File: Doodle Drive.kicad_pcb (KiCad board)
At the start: 2 copper layers, 69.1 x 82.1 mm, 99 parts, among them J1 USB_B, J12 PINHD_1x4_Male, J15 PINHD_1x4_Male, J2 USB_B, J3 Screw_Terminal_01x02, J4 PINHD_1x4_Male, J5 USB_A, J6 PINHD_1x2_Male, J8 PINHD_1x4_Male, J9 PINHD_1x4_Male, U1 STM32F411RETx, U2 DRV8825PWP, U3 DRV8825PWP, U4 DRV8825PWP, U5 DRV8825PWP, U6 AP7343-33W5-7, U7 CP2102-GMR, Y1 32.768KHz ±20ppm 12.5pF, Y2 25MHZ 12PF

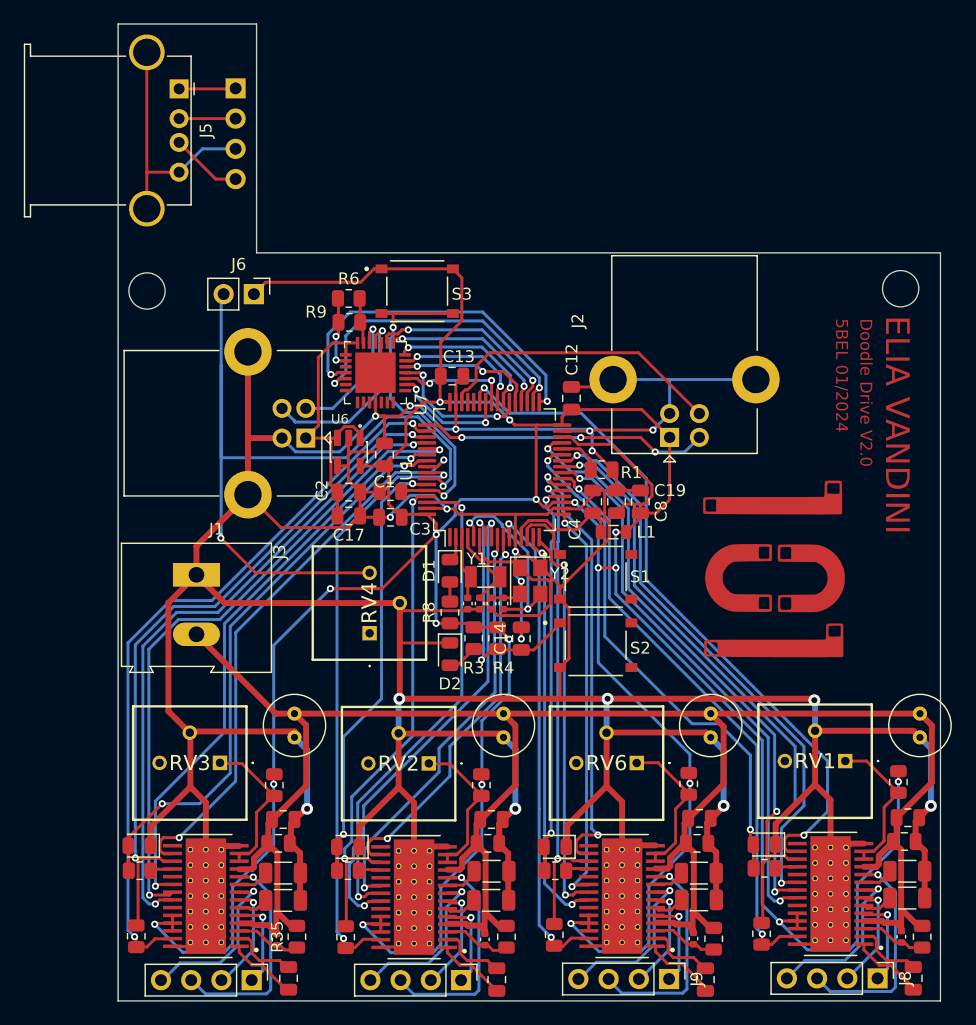
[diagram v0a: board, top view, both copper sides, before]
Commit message: added pins for motor edge sensors, reroutet driver modules, removed module potentiometer, made everything more compact, fixed labels
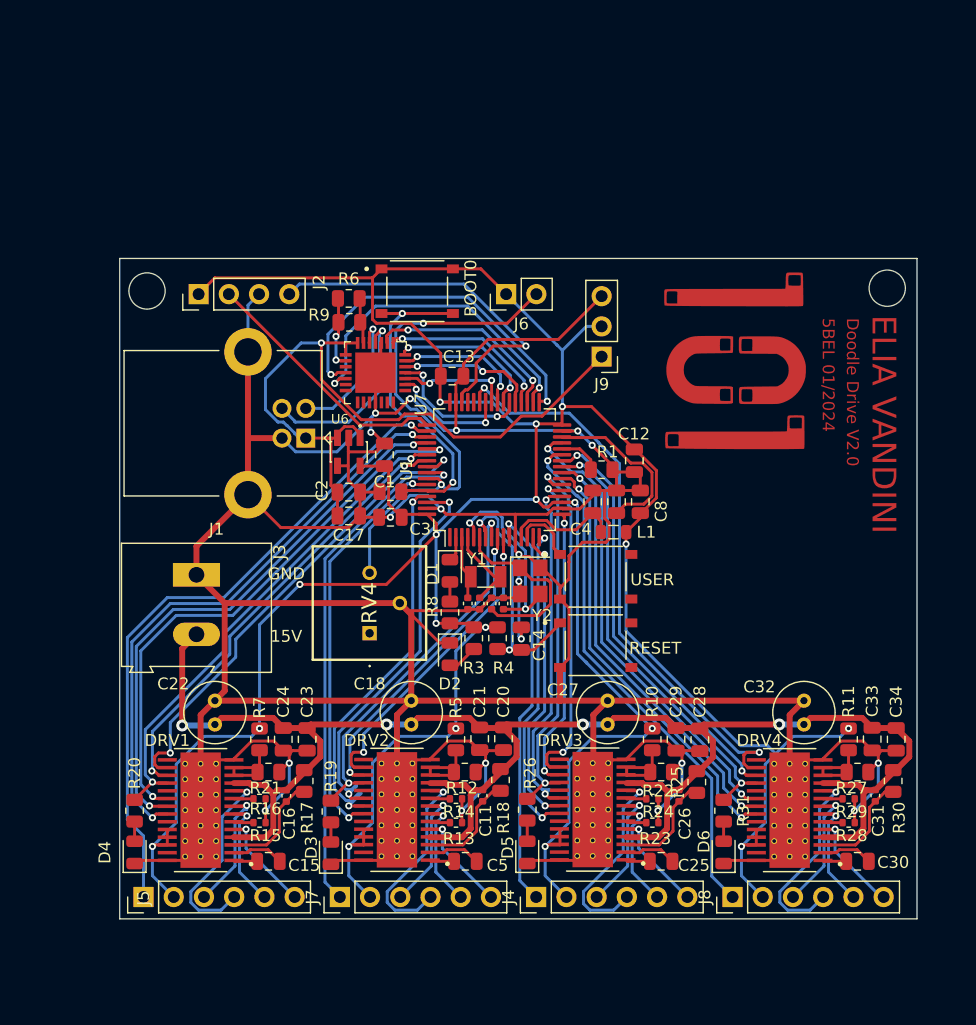
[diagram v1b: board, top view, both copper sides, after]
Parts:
- removed J12, J15: PINHD_1x4_Male, Connector_PinHeader_2.54mm:PinHeader_1x04_P2.54mm_Vertical
- removed R33, R34: 0.1, Resistor_SMD:R_1206_3216Metric
- removed R35: 1M, Resistor_SMD:R_0805_2012Metric
- removed R39: 10k, Resistor_SMD:R_0805_2012Metric
- removed R40: 5.1k, Resistor_SMD:R_0805_2012Metric
- removed RV1, RV2, RV3, RV6: R_Potentiometer, poti:3386P1473LF
- removed U2, U3, U4, U5: DRV8825PWP, DRV8825PWP:IC_TPS61196PWPRQ1
- added DRV1: DRV8825PWP, DRV8825PWP:IC_TPS61196PWPRQ1, F.Cu at (68.0, 98.1)
- added DRV2: DRV8825PWP, DRV8825PWP:IC_TPS61196PWPRQ1, F.Cu at (84.5, 98.1)
- added DRV3: DRV8825PWP, DRV8825PWP:IC_TPS61196PWPRQ1, F.Cu at (101.0, 98.1)
- added DRV4: DRV8825PWP, DRV8825PWP:IC_TPS61196PWPRQ1, F.Cu at (117.5, 98.1)
- added J7: PINHD_1x6_Male, Connector_PinHeader_2.54mm:PinHeader_1x06_P2.54mm_Vertical, F.Cu at (79.8, 105.4)
- added R20: 5.1k, Resistor_SMD:R_0805_2012Metric, F.Cu at (62.5, 98.2)
- added R23: 200m, Resistor_SMD:R_0402_1005Metric, F.Cu at (106.0, 99.2)
- added R27: 10k, Resistor_SMD:R_0805_2012Metric, F.Cu at (123.2, 94.9)
- added R28: 200m, Resistor_SMD:R_0402_1005Metric, F.Cu at (122.5, 99.2)
- added R29: 200m, Resistor_SMD:R_0402_1005Metric, F.Cu at (122.5, 97.2)
- J2: value USB_B -> PINHD_1x4_Male; footprint Connector_USB:USB_B_Lumberg_2411_02_Horizontal -> Connector_PinHeader_2.54mm:PinHeader_1x04_P2.54mm_Vertical
- J4: value PINHD_1x4_Male -> PINHD_1x6_Male; footprint Connector_PinHeader_2.54mm:PinHeader_1x04_P2.54mm_Vertical -> Connector_PinHeader_2.54mm:PinHeader_1x06_P2.54mm_Vertical; moved to F.Cu
- J5: value USB_A -> PINHD_1x6_Male; footprint Connector_USB:USB_A_Stewart_SS-52100-001_Horizontal -> Connector_PinHeader_2.54mm:PinHeader_1x06_P2.54mm_Vertical
- J8: value PINHD_1x4_Male -> PINHD_1x6_Male; footprint Connector_PinHeader_2.54mm:PinHeader_1x04_P2.54mm_Vertical -> Connector_PinHeader_2.54mm:PinHeader_1x06_P2.54mm_Vertical
- J9: value PINHD_1x4_Male -> PINHD_1x3_Male; footprint Connector_PinHeader_2.54mm:PinHeader_1x04_P2.54mm_Vertical -> Connector_PinHeader_2.54mm:PinHeader_1x03_P2.54mm_Vertical
- R10, R11, R5, R7: value 1k -> 3.6k
- R12: value 0.1 -> 10k; footprint Resistor_SMD:R_1206_3216Metric -> Resistor_SMD:R_0805_2012Metric
- R13, R15, R16, R24: value 0.1 -> 200m; footprint Resistor_SMD:R_1206_3216Metric -> Resistor_SMD:R_0402_1005Metric
- R14: value 1M -> 200m; footprint Resistor_SMD:R_0805_2012Metric -> Resistor_SMD:R_0402_1005Metric
- R18, R30: value 10k -> 1M
- R22: value 5.1k -> 10k
- R25: value 0.1 -> 1M; footprint Resistor_SMD:R_1206_3216Metric -> Resistor_SMD:R_0805_2012Metric
- R26: value 1M -> 5.1k
- R8: value 1k -> 5.1k
- moved J4 72.5 mm to (96.2, 105.4), turned to 90 degrees
- moved J5 68.0 mm to (63.2, 105.4), turned to 90 degrees
- moved C34 52.6 mm to (126.5, 92.2), turned to -90 degrees
- moved J9 52.6 mm to (101.8, 60.0), turned to 180 degrees
- moved C31 51.7 mm to (124.8, 96.9)
- moved C33 50.0 mm to (124.5, 92.1), turned to -90 degrees
- moved D6 49.1 mm to (112.0, 101.7), turned to 90 degrees
- moved C30 48.8 mm to (123.2, 102.4), turned to 180 degrees
- moved R11 48.4 mm to (122.5, 92.2)
- moved R30 47.8 mm to (126.2, 95.7), turned to 90 degrees
- moved C32 42.9 mm to (118.8, 88.9), turned to -90 degrees
- moved C18 42.9 mm to (85.8, 88.9), turned to -90 degrees
- moved C22 41.8 mm to (69.2, 88.9), turned to -90 degrees
- moved J2 41.4 mm to (67.9, 54.8)
- moved R14 40.9 mm to (89.5, 97.2), turned to 0 degrees
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- renumbered S3 to BOOT0, S2 to RESET, S1 to USER
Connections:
- C11 pad 2: Net-(U2-VCP) -> Net-(DRV2-VCP)
- C26 pad 2: Net-(U4-VCP) -> Net-(DRV3-VCP)
- C31 pad 2: Net-(U5-VCP) -> Net-(DRV4-VCP)
- C6 pad 2: PH1 -> PH0
- C9 pad 2: PH0 -> PH1
- D3 pad 2: PB1 -> Net-(D3-A)
- D4 pad 2: PA4 -> Net-(D4-A)
- D5 pad 2: PB7 -> Net-(D5-A)
- D6 pad 2: PB3 -> Net-(D6-A)
- J2 pad 3: PA13 -> GND
- J2 pad 4: GND -> PA13
- J4 pad 1: Net-(J5-VBUS) -> PC3
- J4 pad 2: Net-(J5-D-) -> +3V3
- J4 pad 3: Net-(J5-GND) -> Net-(DRV3-BOUT2)
- J4 pad 4: Net-(J5-D+) -> Net-(DRV3-BOUT1)
- J5 pad 1: Net-(J5-VBUS) -> PA15
- J5 pad 2: Net-(J5-D-) -> +3V3
- J5 pad 3: Net-(J5-D+) -> Net-(DRV1-BOUT2)
- J5 pad 4: Net-(J5-GND) -> Net-(DRV1-BOUT1)
- J5 pad 5: Net-(J5-GND) -> Net-(DRV1-AOUT2)
- J8 pad 1: Net-(U2-AOUT1) -> PB1
- J8 pad 2: Net-(U2-AOUT2) -> +3V3
- J9 pad 1: Net-(U3-AOUT1) -> +5V
- J9 pad 2: Net-(U3-AOUT2) -> +3V3
- J9 pad 3: Net-(U3-BOUT1) -> GND
- R10 pad 1: Net-(U4-AVREF) -> Net-(DRV3-AVREF)
- R12 pad 1: Net-(U2-ISENA) -> GND
- R12 pad 2: GND -> Net-(DRV2-AVREF)
- R13 pad 1: GND -> Net-(DRV2-ISENA)
- R13 pad 2: Net-(U2-ISENB) -> GND
- R14 pad 1: Net-(U2-VCP) -> Net-(DRV2-ISENB)
- R14 pad 2: +15V -> GND
- R16 pad 1: GND -> Net-(DRV1-ISENB)
- R16 pad 2: Net-(U3-ISENB) -> GND
- R18 pad 1: PB10 -> Net-(DRV2-VCP)
- R18 pad 2: PA7 -> +15V
- R19 pad 1: PB1 -> PC0
- R19 pad 2: Net-(U2-NFAULT) -> Net-(D3-A)
- R21 pad 1: PA5 -> GND
- R21 pad 2: PC3 -> Net-(DRV1-AVREF)
- R22 pad 1: PA4 -> GND
- R22 pad 2: Net-(U3-NFAULT) -> Net-(DRV3-AVREF)
- R25 pad 1: GND -> Net-(DRV3-VCP)
- R25 pad 2: Net-(U4-ISENB) -> +15V
- R26 pad 1: Net-(U4-VCP) -> PA5
- R26 pad 2: +15V -> Net-(D5-A)
- R30 pad 1: PB8 -> Net-(DRV4-VCP)
- R30 pad 2: PB5 -> +15V
- R31 pad 1: PB7 -> PC5
- R31 pad 2: Net-(U4-NFAULT) -> Net-(D6-A)
- R5 pad 1: Net-(U2-AVREF) -> Net-(DRV2-AVREF)
- R7 pad 1: Net-(U3-AVREF) -> Net-(DRV1-AVREF)
- U1 pad 17: DIR1 -> PA3
- U1 pad 20: PA4 -> DIR3
- U1 pad 26: DIR2 -> PB0
- U1 pad 29: PB10 -> DIR4
- U1 pad 53: PC12 -> DIR1
- U1 pad 54: DIR4 -> PD2
- U1 pad 62: PB9 -> DIR2
- U1 pad 9: DIR3 -> PC1
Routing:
- net PC12: track 55.2 -> 0.00 mm, vias 2 -> 0
- net PB10: track 53.5 -> 0.00 mm, vias 2 -> 0
- net GND: track 505.2 -> 454.0 mm, vias 18 -> 19
- net PB9: track 42.9 -> 0.00 mm, vias 2 -> 0
- net PD2: track 0.00 -> 42.1 mm, vias 0 -> 2
- net +15V: track 184.5 -> 145.5 mm, vias 0 -> 4
- net +5V: track 25.2 -> 62.0 mm, vias 0 -> 1
- net PB0: track 0.00 -> 35.3 mm, vias 0 -> 2
- net PA4: track 35.2 -> 0.00 mm, vias 2 -> 0
- net PC1: track 0.00 -> 26.1 mm, vias 0 -> 2
- net PB6: track 69.0 -> 43.0 mm
- net PA3: track 0.00 -> 23.7 mm, vias 0 -> 2
- net +3V3: track 334.0 -> 310.8 mm, vias 19 -> 18
- net Net-(J5-GND): track 21.4 -> 0.00 mm
- net Net-(U3-BOUT1): track 18.4 -> 0.00 mm, vias 1 -> 0
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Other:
- board size 69.1 x 82.1 mm -> 67 x 55.5 mm
- board text added: "15V"
- board text added: "5V"
- board text added: "AOUT1"
- board text added: "AOUT2"
- board text added: "BOUT1"
- board text added: "BOUT2"
- board text added: "SENSOR"
- board text removed: "CKL"
- board text removed: "IO"
- board text removed: "SWIO"
- board text removed: "TOP"

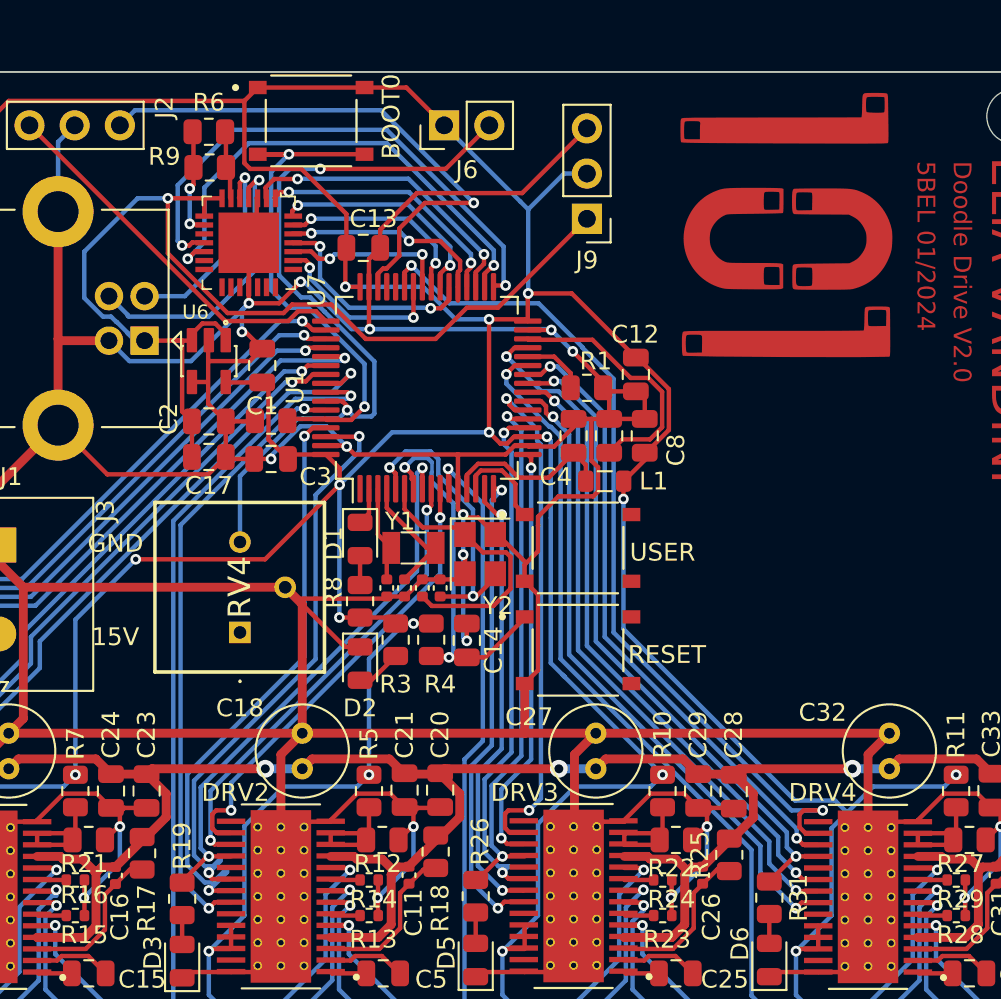
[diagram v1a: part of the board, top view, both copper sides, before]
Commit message: fixed Serial connection, and various improvments
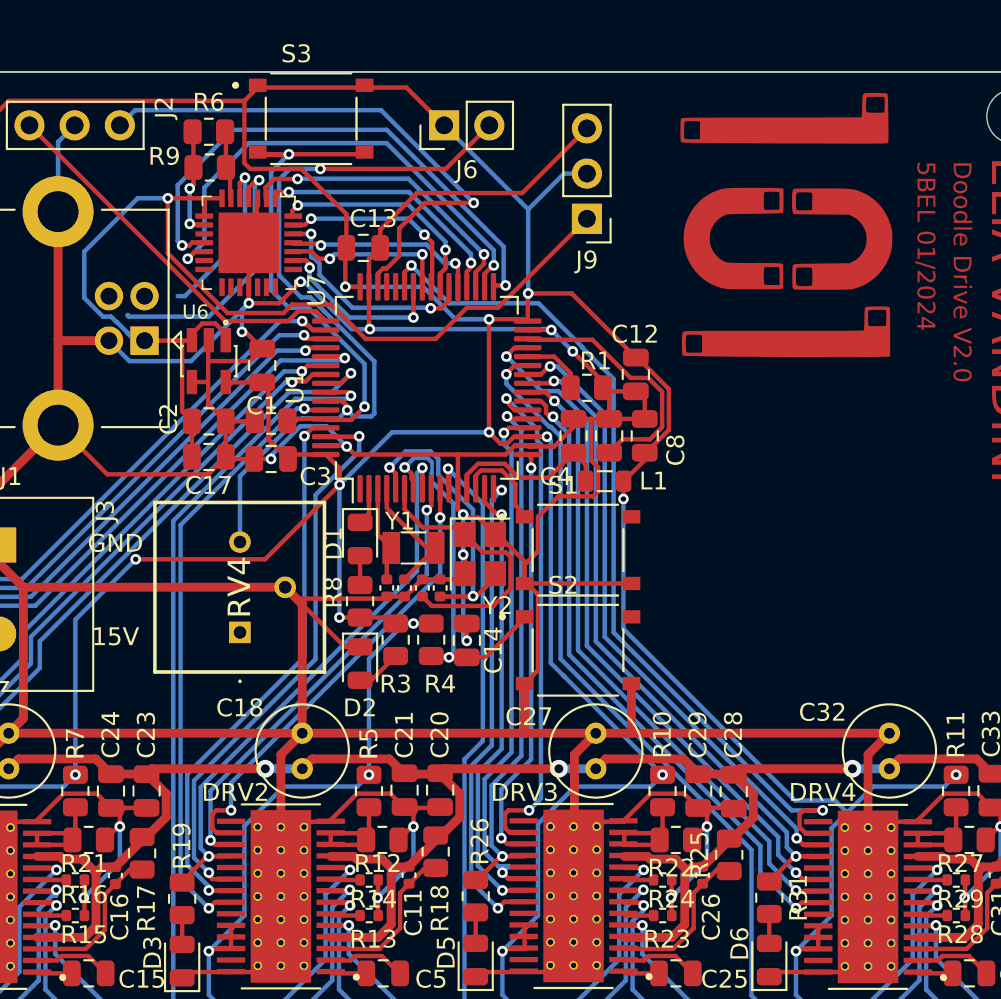
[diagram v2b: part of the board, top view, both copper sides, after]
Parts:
- removed BOOT0, RESET, USER: TS-1187A-B-A-B, TS-1187A-B-A-B:SW_TS-1187A-B-A-B
- added S1: TS-1187A-B-A-B, TS-1187A-B-A-B:SW_TS-1187A-B-A-B, F.Cu at (101.2, 78.6)
- added S2: TS-1187A-B-A-B, TS-1187A-B-A-B:SW_TS-1187A-B-A-B, F.Cu at (101.2, 84.2)
- added S3: TS-1187A-B-A-B, TS-1187A-B-A-B:SW_TS-1187A-B-A-B, F.Cu at (86.2, 54.4)
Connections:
- U7 pad 25: PC7 -> PC6
- U7 pad 26: PC6 -> PC7
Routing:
- net GND: track 454.0 -> 462.8 mm
- net PB8: track 34.1 -> 31.4 mm
- net Net-(J1-D-): track 11.7 -> 9.79 mm
- net DIR2: track 33.7 -> 32.1 mm
- net Net-(J1-D+): track 16.3 -> 14.8 mm
- net PC6: track 12.4 -> 11.9 mm

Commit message: letzter code
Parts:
- removed S1, S2, S3: TS-1187A-B-A-B, TS-1187A-B-A-B:SW_TS-1187A-B-A-B
- C26: value 100nF -> 10nF; footprint Capacitor_SMD:C_0402_1005Metric -> Capacitor_SMD:C_0805_2012Metric
- C27: value 10uF -> 100nF; footprint Capacitor_THT:C_Radial_D5.0mm_H5.0mm_P2.00mm -> Capacitor_SMD:C_0402_1005Metric
- C28: footprint Capacitor_SMD:C_0805_2012Metric -> Capacitor_SMD:C_0402_1005Metric
- C29: value 100nF -> 10uF; footprint Capacitor_SMD:C_0805_2012Metric -> Capacitor_THT:C_Radial_D5.0mm_H5.0mm_P2.00mm
- C30: value 10nF -> 10uF; footprint Capacitor_SMD:C_0805_2012Metric -> Capacitor_THT:C_Radial_D5.0mm_H5.0mm_P2.00mm
- C31: footprint Capacitor_SMD:C_0402_1005Metric -> Capacitor_SMD:C_0805_2012Metric
- C32: value 10uF -> 100nF; footprint Capacitor_THT:C_Radial_D5.0mm_H5.0mm_P2.00mm -> Capacitor_SMD:C_0805_2012Metric
- R10, R5, R7: value 3.6k -> 15k
- R11: value 3.6k -> 9.1k
- R12, R21: value 10k -> 9.1k
- R13, R14, R15, R16, R24: value 200m -> 100m; footprint Resistor_SMD:R_0402_1005Metric -> Resistor_SMD:R_1206_3216Metric
- R22: value 10k -> 15k
- R23: value 200m -> 9.1k; footprint Resistor_SMD:R_0402_1005Metric -> Resistor_SMD:R_0805_2012Metric
- R25: value 1M -> 100m; footprint Resistor_SMD:R_0805_2012Metric -> Resistor_SMD:R_1206_3216Metric
- R26: value 5.1k -> 100m; footprint Resistor_SMD:R_0805_2012Metric -> Resistor_SMD:R_1206_3216Metric
- R27: value 10k -> 100m; footprint Resistor_SMD:R_0805_2012Metric -> Resistor_SMD:R_1206_3216Metric
- R28, R29: value 200m -> 1M; footprint Resistor_SMD:R_0402_1005Metric -> Resistor_SMD:R_0805_2012Metric
- R30: value 1M -> 5.1k
- moved C30 25.5 mm to (100.8, 90.2), turned to 0 degrees
- moved C27 24.3 mm to (123.4, 100.8), turned to 180 degrees
- moved C34 18.3 mm to (108.2, 92.2), turned to 0 degrees
- moved R24 17.8 mm to (123.7, 98.8)
- moved D6 16.8 mm to (95.2, 101.9)
- moved R31 16.8 mm to (95.2, 98.3)
- moved J8 16.7 mm to (96.0, 105.4)
- moved J4 16.3 mm to (112.5, 105.4)
- moved D5 16.3 mm to (111.8, 101.9)
- moved R27 16.2 mm to (107.2, 96.5), turned to 0 degrees
- moved R10 16.0 mm to (121.9, 93.2)
- moved C25 15.9 mm to (122.7, 102.6), turned to 0 degrees
- moved R30 14.7 mm to (111.8, 98.3), turned to -90 degrees
- moved R29 14.4 mm to (108.9, 101.9), turned to 90 degrees
- moved R25 14.0 mm to (123.7, 96.5), turned to 0 degrees
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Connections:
- C25 pad 1: Net-(DRV3-CP2) -> Net-(DRV4-CP2)
- C25 pad 2: Net-(DRV3-CP1) -> Net-(DRV4-CP1)
- C26 pad 1: +15V -> Net-(DRV3-CP2)
- C26 pad 2: Net-(DRV3-VCP) -> Net-(DRV3-CP1)
- C27 pad 1: GND -> +15V
- C27 pad 2: +15V -> Net-(DRV4-VCP)
- C28 pad 2: GND -> Net-(DRV3-VCP)
- C29 pad 1: +15V -> GND
- C29 pad 2: GND -> +15V
- C30 pad 1: Net-(DRV4-CP2) -> GND
- C30 pad 2: Net-(DRV4-CP1) -> +15V
- C31 pad 2: Net-(DRV4-VCP) -> GND
- C32 pad 1: GND -> +15V
- C32 pad 2: +15V -> GND
- DRV1 pad 16: PB4 -> PB3
- DRV1 pad 17: PB3 -> PD2
- DRV1 pad 18: PD2 -> PB4
- J4 pad 1: PC3 -> PB1
- J4 pad 3: Net-(DRV3-BOUT2) -> Net-(DRV4-BOUT2)
- J4 pad 4: Net-(DRV3-BOUT1) -> Net-(DRV4-BOUT1)
- J4 pad 5: Net-(DRV3-AOUT2) -> Net-(DRV4-AOUT2)
- J4 pad 6: Net-(DRV3-AOUT1) -> Net-(DRV4-AOUT1)
- J8 pad 1: PB1 -> PC3
- J8 pad 3: Net-(DRV4-BOUT2) -> Net-(DRV3-BOUT2)
- J8 pad 4: Net-(DRV4-BOUT1) -> Net-(DRV3-BOUT1)
- J8 pad 5: Net-(DRV4-AOUT2) -> Net-(DRV3-AOUT2)
- J8 pad 6: Net-(DRV4-AOUT1) -> Net-(DRV3-AOUT1)
- R10 pad 1: Net-(DRV3-AVREF) -> Net-(DRV4-AVREF)
- R11 pad 1: Net-(DRV4-AVREF) -> GND
- R11 pad 2: +3V3 -> Net-(DRV4-AVREF)
- R20 pad 1: PD2 -> PB4
- R22 pad 1: GND -> Net-(DRV3-AVREF)
- R22 pad 2: Net-(DRV3-AVREF) -> +3V3
- R23 pad 1: Net-(DRV3-ISENA) -> GND
- R23 pad 2: GND -> Net-(DRV3-AVREF)
- R24 pad 1: Net-(DRV3-ISENB) -> Net-(DRV4-ISENA)
- R25 pad 1: Net-(DRV3-VCP) -> Net-(DRV4-ISENB)
- R25 pad 2: +15V -> GND
- R26 pad 1: PA5 -> Net-(DRV3-ISENA)
- R26 pad 2: Net-(D5-A) -> GND
- R27 pad 1: GND -> Net-(DRV3-ISENB)
- R27 pad 2: Net-(DRV4-AVREF) -> GND
- R28 pad 1: Net-(DRV4-ISENA) -> Net-(DRV4-VCP)
- R28 pad 2: GND -> +15V
- R29 pad 1: Net-(DRV4-ISENB) -> Net-(DRV3-VCP)
- R29 pad 2: GND -> +15V
- R30 pad 1: Net-(DRV4-VCP) -> PC5
- R30 pad 2: +15V -> Net-(D5-A)
- R31 pad 1: PC5 -> PA5
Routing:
- net GND: track 462.8 -> 416.0 mm, vias 19 -> 6
- net +15V: track 145.5 -> 168.1 mm, vias 4 -> 6
- net +3V3: track 310.8 -> 325.3 mm, vias 18 -> 20
- net +5V: track 62.0 -> 52.6 mm
- net Net-(U1-VCAP1): track 14.3 -> 7.04 mm
- net BOOT0: track 29.9 -> 26.7 mm
- net PB4: track 40.5 -> 43.6 mm
- net ~{RST}: track 22.2 -> 19.3 mm
- net PD2: track 42.1 -> 39.3 mm
- net Net-(DRV3-CP1): track 1.98 -> 4.59 mm
- net Net-(DRV2-CP1): track 1.98 -> 4.59 mm
- net Net-(DRV4-CP1): track 1.98 -> 4.59 mm
- net Net-(DRV1-CP1): track 1.98 -> 4.59 mm
- net Net-(DRV4-VCP): track 8.91 -> 6.54 mm
- net Net-(DRV3-VCP): track 8.91 -> 6.54 mm
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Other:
- board size 67 x 55.5 mm -> 66 x 55.5 mm
- board text removed: "AOUT1"
- board text removed: "AOUT2"
- board text removed: "BOUT1"
- board text removed: "BOUT2"
